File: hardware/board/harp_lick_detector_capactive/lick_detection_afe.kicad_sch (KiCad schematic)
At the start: 46 parts, among them J3 Conn_Triaxial, U13 ADS7049, U6 LTC6263, U7 LTC6268xS8-10, U8 REF2033

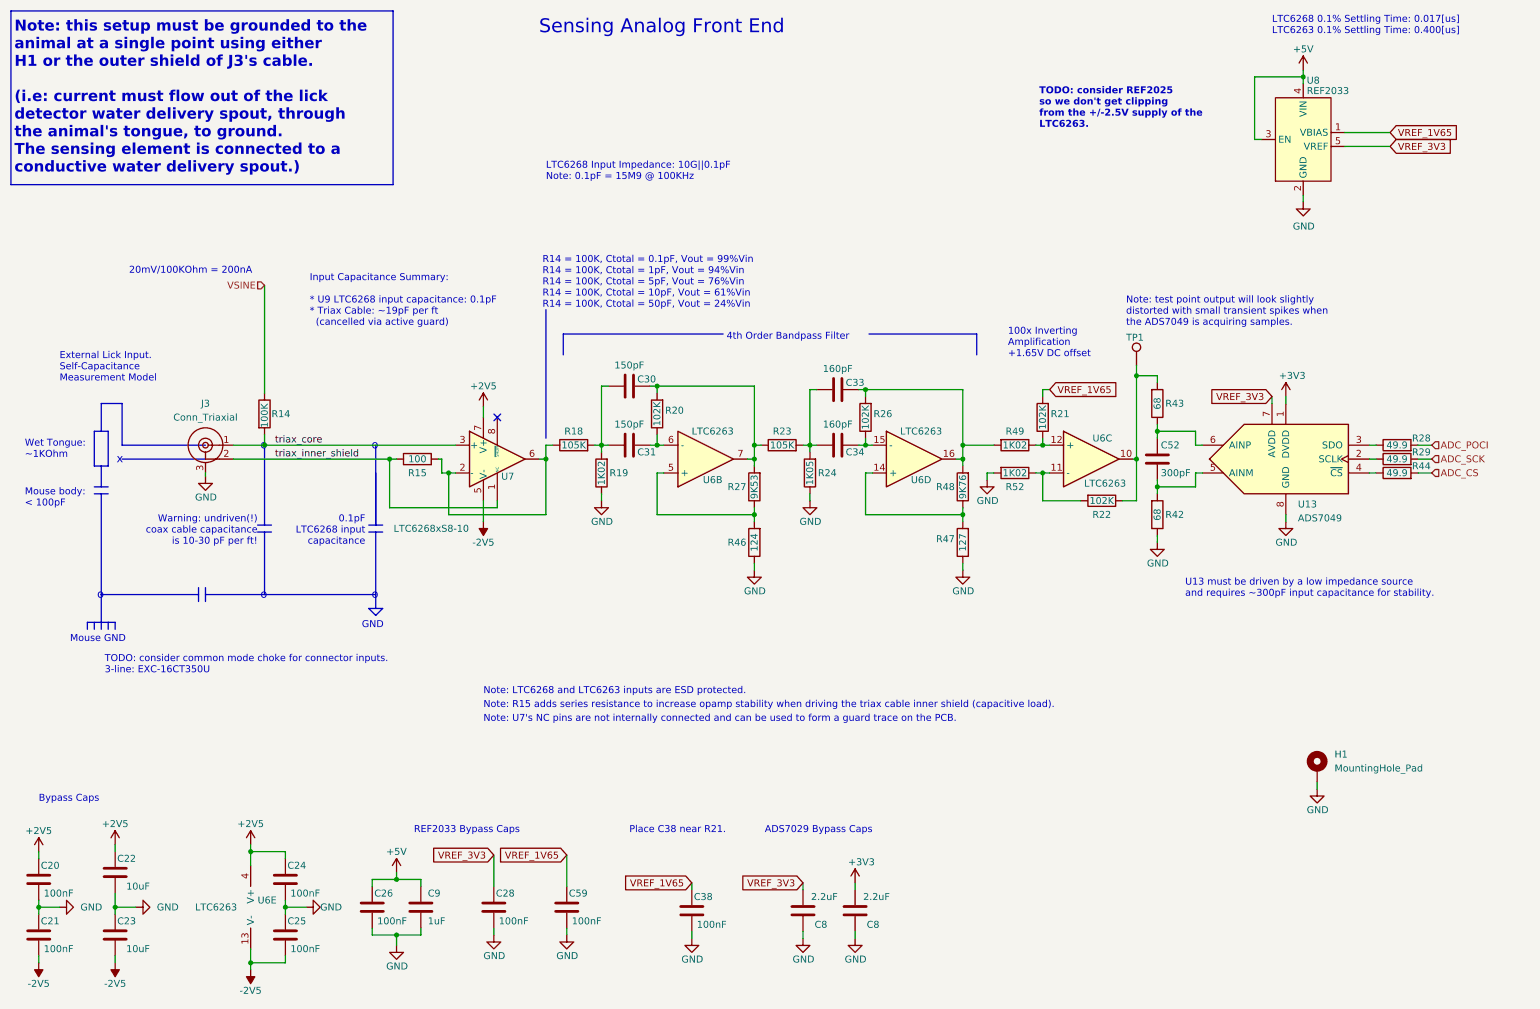
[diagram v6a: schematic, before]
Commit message: update layout for v0.6.1
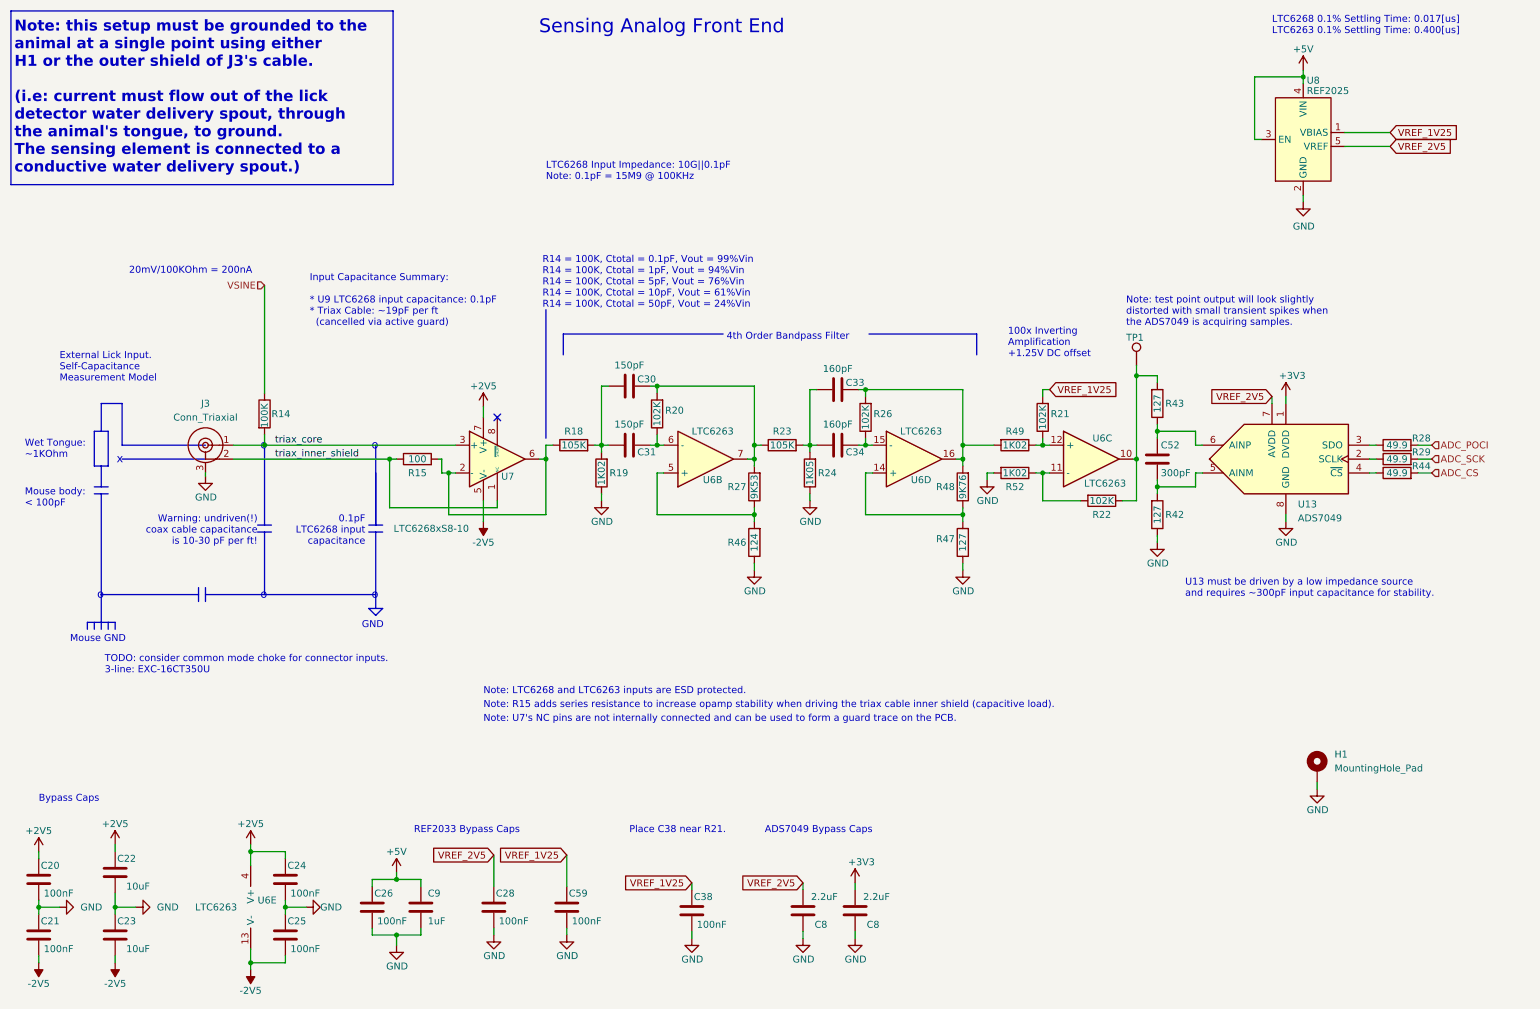
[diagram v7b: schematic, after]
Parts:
- H1: Link https://www.digikey.com/en/products/detail/keystone-electronics/7794/2171012 -> https://www.digikey.com/en/products/detail/keystone-electronics/7792/2171011; Manufacturer Number 7794 -> 7792
- R42, R43: value 68 -> 127; Link https://www.digikey.com/en/products/detail/yageo/RT0402BRD0768RL/1069370 -> https://www.digikey.com/en/products/detail/yageo/RT0402BRD07127RL/1069018; Manufacturer Number RT0402BRD0768RL -> RT0402BRD07127RL; Temperature Coefficient 25ppm/C -> (none)
- TP1: footprint kicad_component_library:TestPoint_Keystone_5027_Miniature -> TestPoint:TestPoint_THTPad_D3.0mm_Drill1.5mm; Link https://www.digikey.com/en/products/detail/keystone-electro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 -> (none); Manufacturer Keystone Electronics -> (none); Manufacturer Number 5027 -> (none); Notes SMT testpoint with hole for added sturdiness. -> (none)
- U8: value REF2033 -> REF2025; Link https://www.digikey.com/en/products/detail/texas-instruments/REF2033AIDDCT/4946346 -> https://www.digikey.com/en/products/detail/texas-instruments/REF2025AISDDCR/9489207; Manufacturer Number REF2033AIDDCT -> REF2025AISDDCR; Notes (none) -> 1.25V/2.5V dual voltage reference
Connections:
- net VREF_1V65 renamed VREF_1V25
- net VREF_3V3 renamed VREF_2V5
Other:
- note added: "100x Inverting Amplification +1.25V DC offset"
- note added: "ADS7049 Bypass Caps"
- note removed: "100x Inverting Amplification +1.65V DC offset"
- note removed: "ADS7029 Bypass Caps"
- note removed: "TODO: consider REF2025 so we don't get clipping from the +/-2.5V supply of the LTC6263."
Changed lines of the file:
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@@
     (effects (font (size 1.5 1.5)) (justify left bottom))
   )
-  (text "100x Inverting \nAmplification\n+1.65V DC offset" (at 195.58 78.74 0)
+  (text "100x Inverting \nAmplification\n+1.25V DC offset" (at 195.58 78.74 0)
     (effects (font (size 1.27 1.27)) (justify left bottom))
   )
@@
     (effects (font (size 2 2) (thickness 0.254) bold) (justify left bottom))
   )
-  (text "TODO: consider REF2025\nso we don't get clipping\nfrom the +/-2.5V supply of the\nLTC6263."
-    (at 201.295 36.83 0)
-    (effects (font (size 1.27 1.27) (thickness 0.254) bold) (justify left bottom))
-  )
   (text "Note: LTC6268 and LTC6263 inputs are ESD protected."
     (at 99.695 140.335 0)
@@
     (effects (font (size 1.27 1.27)) (justify right bottom))
   )
-  (text "ADS7029 Bypass Caps" (at 151.13 165.735 0)
+  (text "ADS7049 Bypass Caps" (at 151.13 165.735 0)
     (effects (font (size 1.27 1.27)) (justify left bottom))
   )
@@
     (effects (font (size 1.27 1.27)) (justify left bottom))
   )
-  (global_label "VREF_1V65" (shape input) (at 114.935 169.545 180) (fields_autoplaced)
+  (global_label "VREF_1V25" (shape input) (at 114.935 169.545 180) (fields_autoplaced)
     (effects (font (size 1.27 1.27)) (justify right))
     (property "Intersheetrefs" "${INTERSHEET_REFS}" (at 101.6689 169.545 0)
@@
     )
   )
-  (global_label "VREF_3V3" (shape input) (at 101.6 169.545 180) (fields_autoplaced)
+  (global_label "VREF_2V5" (shape input) (at 101.6 169.545 180) (fields_autoplaced)
     (effects (font (size 1.27 1.27)) (justify right))
     (property "Intersheetrefs" "${INTERSHEET_REFS}" (at 89.5434 169.545 0)
@@
     )
   )
-  (global_label "VREF_1V65" (shape input) (at 265.43 37.465 0) (fields_autoplaced)
+  (global_label "VREF_1V25" (shape input) (at 265.43 37.465 0) (fields_autoplaced)
     (effects (font (size 1.27 1.27)) (justify left))
     (property "Intersheetrefs" "${INTERSHEET_REFS}" (at 278.6961 37.465 0)
@@
     )
   )
-  (global_label "VREF_3V3" (shape input) (at 265.43 40.005 0) (fields_autoplaced)
+  (global_label "VREF_2V5" (shape input) (at 265.43 40.005 0) (fields_autoplaced)
     (effects (font (size 1.27 1.27)) (justify left))
     (property "Intersheetrefs" "${INTERSHEET_REFS}" (at 277.4866 40.005 0)
@@
     )
   )
-  (global_label "VREF_3V3" (shape input) (at 158.115 174.625 180) (fields_autoplaced)
+  (global_label "VREF_2V5" (shape input) (at 158.115 174.625 180) (fields_autoplaced)
     (effects (font (size 1.27 1.27)) (justify right))
     (property "Intersheetrefs" "${INTERSHEET_REFS}" (at 146.0584 174.625 0)
@@
     )
   )
-  (global_label "VREF_1V65" (shape input) (at 137.795 174.625 180) (fields_autoplaced)
+  (global_label "VREF_1V25" (shape input) (at 137.795 174.625 180) (fields_autoplaced)
     (effects (font (size 1.27 1.27)) (justify right))
     (property "Intersheetrefs" "${INTERSHEET_REFS}" (at 124.5289 174.625 0)
@@
     )
   )
-  (global_label "VREF_1V65" (shape input) (at 203.2 84.455 0) (fields_autoplaced)
+  (global_label "VREF_1V25" (shape input) (at 203.2 84.455 0) (fields_autoplaced)
     (effects (font (size 1.27 1.27)) (justify left))
     (property "Intersheetrefs" "${INTERSHEET_REFS}" (at 216.4661 84.455 0)
@@
     )
   )
-  (global_label "VREF_3V3" (shape input) (at 243.84 85.725 180) (fields_autoplaced)
+  (global_label "VREF_2V5" (shape input) (at 243.84 85.725 180) (fields_autoplaced)
     (effects (font (size 1.27 1.27)) (justify right))
     (property "Intersheetrefs" "${INTERSHEET_REFS}" (at 231.7834 85.725 0)
@@
       (effects (font (size 1.27 1.27)) (justify left))
     )
-    (property "Value" "REF2033" (at 250.19 29.845 0)
+    (property "Value" "REF2025" (at 250.19 29.845 0)
       (effects (font (size 1.27 1.27)) (justify left))
     )
@@
       (effects (font (size 1.27 1.27)) hide)
     )
-    (property "Manufacturer Number" "REF2033AIDDCT" (at 249.555 38.735 0)
-      (effects (font (size 1.27 1.27)) hide)
-    )
-    (property "Link" "https://www.digikey.com/en/products/detail/texas-instruments/REF2033AIDDCT/4946346" (at 249.555 38.735 0)
+    (property "Manufacturer Number" "REF2025AISDDCR" (at 249.555 38.735 0)
+      (effects (font (size 1.27 1.27)) hide)
+    )
+    (property "Link" "https://www.digikey.com/en/products/detail/texas-instruments/REF2025AISDDCR/9489207" (at 249.555 38.735 0)
+      (effects (font (size 1.27 1.27)) hide)
+    )
+    (property "Notes" "1.25V/2.5V dual voltage reference" (at 249.555 38.735 0)
       (effects (font (size 1.27 1.27)) hide)
     )
@@
       (effects (font (size 1.27 1.27)))
     )
-    (property "Value" "68" (at 222.885 107.315 90)
+    (property "Value" "127" (at 222.885 107.315 90)
       (effects (font (size 1.27 1.27)))
     )
@@
       (effects (font (size 1.27 1.27)) hide)
     )
-    (property "Link" "https://www.digikey.com/en/products/detail/yageo/RT0402BRD0768RL/1069370" (at 222.885 107.315 0)
+    (property "Link" "https://www.digikey.com/en/products/detail/yageo/RT0402BRD07127RL/1069018" (at 222.885 107.315 0)
       (effects (font (size 1.27 1.27)) hide)
     )
@@
       (effects (font (size 1.27 1.27)) hide)
     )
-    (property "Manufacturer Number" "RT0402BRD0768RL" (at 222.885 107.315 0)
+    (property "Manufacturer Number" "RT0402BRD07127RL" (at 222.885 107.315 0)
       (effects (font (size 1.27 1.27)) hide)
     )
@@
       (effects (font (size 1.27 1.27)) hide)
     )
-    (property "Temperature Coefficient" "25ppm/C" (at 222.885 107.315 90)
+    (property "Temperature Coefficient" "" (at 222.885 107.315 90)
       (effects (font (size 1.27 1.27)) hide)
     )
@@
       (effects (font (size 1.27 1.27)) hide)
     )
-    (property "Link" "https://www.digikey.com/en/products/detail/keystone-electronics/7794/2171012" (at 252.095 153.67 0)
-      (effects (font (size 1.27 1.27)) hide)
-    )
-    (property "Manufacturer Number" "7794" (at 252.095 153.67 0)
+    (property "Link" "https://www.digikey.com/en/products/detail/keystone-electronics/7792/2171011" (at 252.095 153.67 0)
+      (effects (font (size 1.27 1.27)) hide)
+    )
+    (property "Manufacturer Number" "7792" (at 252.095 153.67 0)
       (effects (font (size 1.27 1.27)) hide)
     )
@@
       (effects (font (size 1.27 1.27)) (justify left) hide)
     )
-    (property "Footprint" "kicad_component_library:TestPoint_Keystone_5027_Miniature" (at 224.155 80.01 0)
-      (effects (font (size 1.27 1.27)) hide)
-    )
-    (property "Datasheet" "https://www.keyelco.com/userAssets/file/M65p55.pdf" (at 224.155 80.01 0)
-      (effects (font (size 1.27 1.27)) hide)
-    )
-    (property "Link" "https://www.digikey.com/en/products/detail/keystone-electronics/5027/5118871" (at 219.075 80.01 0)
-      (effects (font (size 1.27 1.27)) hide)
-    )
-    (property "Notes" "SMT testpoint with hole for added sturdiness." (at 219.075 80.01 0)
-      (effects (font (size 1.27 1.27)) hide)
-    )
-    (property "Manufacturer" "Keystone Electronics" (at 219.075 80.01 0)
-      (effects (font (size 1.27 1.27)) hide)
-    )
-    (property "Manufacturer Number" "5027" (at 219.075 80.01 0)
+    (property "Footprint" "TestPoint:TestPoint_THTPad_D3.0mm_Drill1.5mm" (at 224.155 80.01 0)
+      (effects (font (size 1.27 1.27)) hide)
+    )
+    (property "Datasheet" "" (at 224.155 80.01 0)
+      (effects (font (size 1.27 1.27)) hide)
+    )
+    (property "Link" "" (at 219.075 80.01 0)
+      (effects (font (size 1.27 1.27)) hide)
+    )
+    (property "Notes" "" (at 219.075 80.01 0)
+      (effects (font (size 1.27 1.27)) hide)
+    )
+    (property "Manufacturer" "" (at 219.075 80.01 0)
+      (effects (font (size 1.27 1.27)) hide)
+    )
+    (property "Manufacturer Number" "" (at 219.075 80.01 0)
       (effects (font (size 1.27 1.27)) hide)
     )
@@
       (effects (font (size 1.27 1.27)))
     )
-    (property "Value" "68" (at 222.885 86.995 90)
+    (property "Value" "127" (at 222.885 86.995 90)
       (effects (font (size 1.27 1.27)))
     )
@@
       (effects (font (size 1.27 1.27)) hide)
     )
-    (property "Link" "https://www.digikey.com/en/products/detail/yageo/RT0402BRD0768RL/1069370" (at 222.885 86.995 0)
+    (property "Link" "https://www.digikey.com/en/products/detail/yageo/RT0402BRD07127RL/1069018" (at 222.885 86.995 0)
       (effects (font (size 1.27 1.27)) hide)
     )
@@
       (effects (font (size 1.27 1.27)) hide)
     )
-    (property "Manufacturer Number" "RT0402BRD0768RL" (at 222.885 86.995 0)
+    (property "Manufacturer Number" "RT0402BRD07127RL" (at 222.885 86.995 0)
       (effects (font (size 1.27 1.27)) hide)
     )
@@
       (effects (font (size 1.27 1.27)) hide)
     )
-    (property "Temperature Coefficient" "25ppm/C" (at 222.885 86.995 90)
-      (effects (font (size 1.27 1.27)) hide)
-    )
+    (property "Temperature Coefficient" "" (at 222.885 86.995 90)
+      (effects (font (size 1.27 1.27)) hide)
+    )

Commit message: update lickety split 0.6.1 pcb files
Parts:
- C52: Tolerance (none) -> 1%; Tolerlance 1% -> (none)
- R14: Link RT1206FRE07100KL -> https://www.digikey.com/en/products/detail/yageo/RT1206FRE0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; Manufacturer Number https://www.digikey.com/en/products/detail/yageo/RT1206FRE0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 -> RT1206FRE07100KL
- TP1: Manufacturer (none) -> n/a; Manufacturer Number (none) -> n/a
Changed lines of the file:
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@@
       (effects (font (size 1.27 1.27)) hide)
     )
-    (property "Tolerlance" "1%" (at 222.885 97.155 0)
+    (property "Tolerance" "1%" (at 222.885 97.155 0)
       (effects (font (size 1.27 1.27)) hide)
     )
@@
       (effects (font (size 1.27 1.27)) hide)
     )
-    (property "Manufacturer" "" (at 219.075 80.01 0)
-      (effects (font (size 1.27 1.27)) hide)
-    )
-    (property "Manufacturer Number" "" (at 219.075 80.01 0)
+    (property "Manufacturer" "n/a" (at 219.075 80.01 0)
+      (effects (font (size 1.27 1.27)) hide)
+    )
+    (property "Manufacturer Number" "n/a" (at 219.075 80.01 0)
       (effects (font (size 1.27 1.27)) hide)
     )
@@
       (effects (font (size 1.27 1.27)) hide)
     )
-    (property "Link" "RT1206FRE07100KL" (at 59.69 88.9 0)
+    (property "Link" "https://www.digikey.com/en/products/detail/yageo/RT1206FRE07100KL/1082857" (at 59.69 88.9 0)
       (effects (font (size 1.27 1.27)) hide)
     )
@@
       (effects (font (size 1.27 1.27)) hide)
     )
-    (property "Manufacturer Number" "https://www.digikey.com/en/products/detail/yageo/RT1206FRE07100KL/1082857" (at 59.69 88.9 0)
-      (effects (font (size 1.27 1.27)) hide)
-    )
+    (property "Manufacturer Number" "RT1206FRE07100KL" (at 59.69 88.9 0)
+      (effects (font (size 1.27 1.27)) hide)
+    )
